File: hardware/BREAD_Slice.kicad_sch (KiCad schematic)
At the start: 16 parts, among them J10 Screw_Terminal_01x02, J11 Screw_Terminal_01x02, J12 Screw_Terminal_01x02, J13 Screw_Terminal_01x02, J14 Screw_Terminal_01x02, J15 Screw_Terminal_01x02, J16 Screw_Terminal_01x02, J2 Screw_Terminal_01x02, J3 Screw_Terminal_01x02, J4 Screw_Terminal_01x02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

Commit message: update schem
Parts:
- removed J10, J11, J12, J13, J14, J16, J2, J3, J4, J5, J6, J7, J8, J9: Screw_Terminal_01x02, symbol Connector:Screw_Terminal_01x02
- added J2, J3, J4, J5, J6, J7, J8, J9: Screw_Terminal_01x04, symbol Connector:Screw_Terminal_01x04
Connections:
- net GND: now also J2.4 (Pin_4), J3.4 (Pin_4), J4.4 (Pin_4), J5.4 (Pin_4), J6.4 (Pin_4), J7.4 (Pin_4), J8.4 (Pin_4), J9.4 (Pin_4)
- net VOUT renamed VFIELD
- net VFIELD: now also J2.3 (Pin_3), J3.3 (Pin_3), J4.3 (Pin_3), J5.3 (Pin_3), J6.3 (Pin_3), J7.3 (Pin_3), J8.3 (Pin_3), J9.3 (Pin_3)
- new net IN1+: J6.1 (Pin_1)
- new net IN1-: J6.2 (Pin_2)
- new net IN2+: J7.1 (Pin_1)
- new net IN2-: J7.2 (Pin_2)
- new net IN3+: J8.1 (Pin_1)
- new net IN3-: J8.2 (Pin_2)
- new net IN4+: J9.1 (Pin_1)
- new net IN4-: J9.2 (Pin_2)
- new net OUT1+: J2.1 (Pin_1)
- new net OUT1-: J2.2 (Pin_2)
- new net OUT2+: J3.1 (Pin_1)
- new net OUT2-: J3.2 (Pin_2)
- new net OUT3+: J4.1 (Pin_1)
- new net OUT3-: J4.2 (Pin_2)
- new net OUT4+: J5.1 (Pin_1)
- new net OUT4-: J5.2 (Pin_2)
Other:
- moved on the sheet: J15, SW3

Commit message: finalize revision of schematic
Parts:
- removed J2, J3, J4, J5, J6, J7, J8, J9: Screw_Terminal_01x04, symbol Connector:Screw_Terminal_01x04
- added J2, J3: Screw_Terminal_01x12, symbol Connector:Screw_Terminal_01x12
- renumbered J15 to J1, SW3 to SW1
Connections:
- net GND: now also J3.12 (Pin_12), J3.3 (Pin_3), J3.6 (Pin_6), J3.9 (Pin_9)
- net IN1+: now also J3.1 (Pin_1)
- net IN1-: now also J3.2 (Pin_2)
- net IN2+: now also J3.4 (Pin_4)
- net IN2-: now also J3.5 (Pin_5)
- net IN3+: now also J3.7 (Pin_7)
- net IN3-: now also J3.8 (Pin_8)
- net IN4+: now also J3.10 (Pin_10)
- net IN4-: now also J3.11 (Pin_11)
- net OUT1+: now also J2.1 (Pin_1)
- net OUT1-: now also J2.2 (Pin_2)
- net OUT2+: now also J2.4 (Pin_4)
- net OUT2-: now also J2.5 (Pin_5)
- net OUT3+: now also J2.7 (Pin_7)
- net OUT3-: now also J2.8 (Pin_8)
- net OUT4+: now also J2.10 (Pin_10)
- net OUT4-: now also J2.11 (Pin_11)
- net VFIELD: now also J2.12 (Pin_12), J2.3 (Pin_3), J2.6 (Pin_6), J2.9 (Pin_9)
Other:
- sheet Isolated Input1 ports: added VCC; removed none
- sheet Isolated Input2 ports: added VCC; removed none
- sheet Isolated Input3 ports: added VCC; removed none
- sheet Isolated Input4 ports: added VCC; removed none
- note added: "Connect GND to IN− for board-referenced (non-isolated) input at IN+. Leave IN− floating for isolated (floating) input; external source must provide return path."
- note added: "Connect VFIELD to OUTx- for wet (VFIELD) contact at OUTx+. Leave VFIELD disconnected and use OUTx− / OUTx+ for dry contact operation."
- note added: "Field Voltage Input Protection"
- note added: "Opto-Isolated Inputs"
- note added: "Reverse and transient voltage protection for external field voltage input."
- note added: "Solid-State Relay Outputs"
- moved on the sheet: J1, SW1

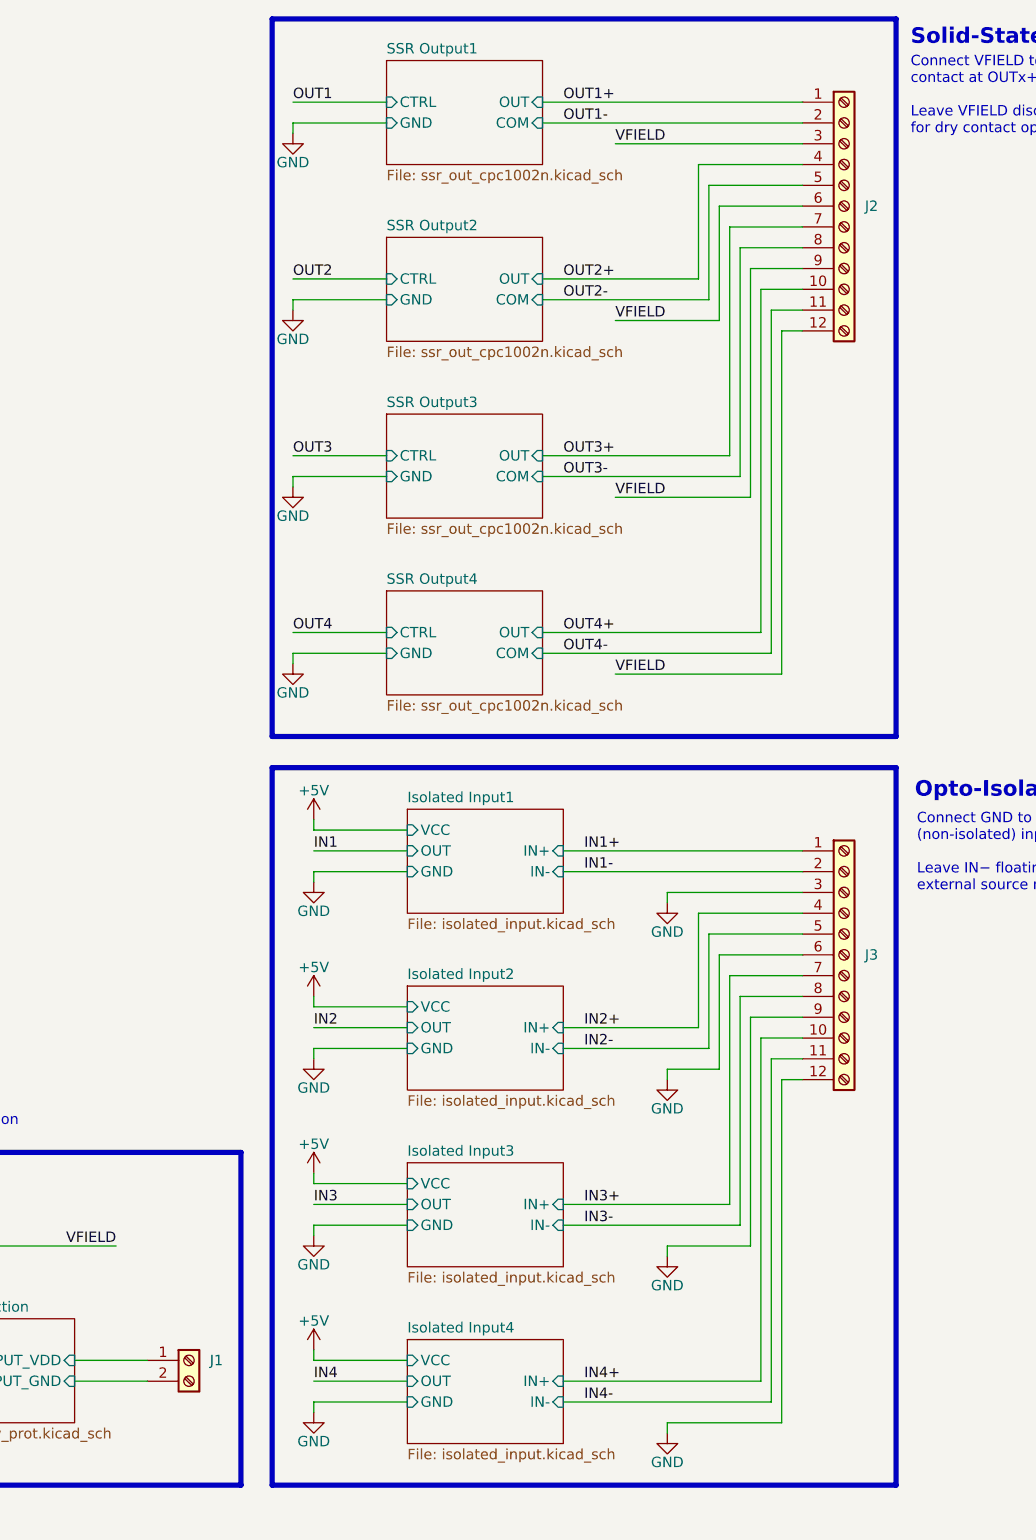
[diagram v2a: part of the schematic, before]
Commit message: revision of symbol attachment and clear out old layout and start new; kml-custom to kmlib-local
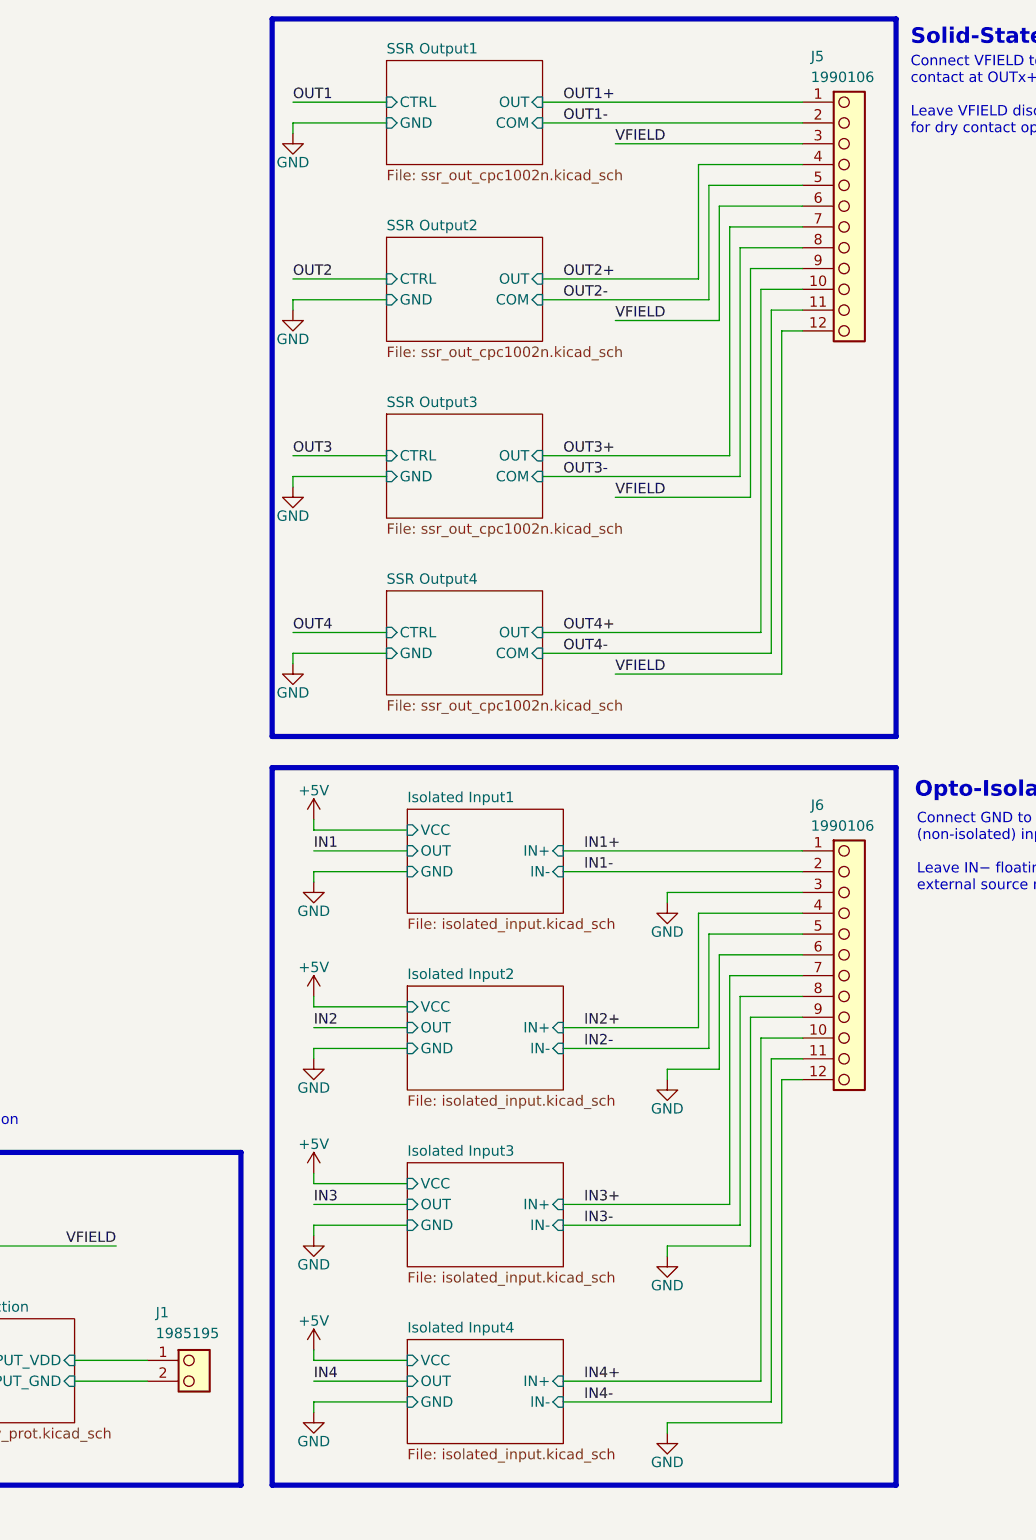
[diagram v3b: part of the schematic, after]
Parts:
- removed J1: Screw_Terminal_01x02, symbol Connector:Screw_Terminal_01x02
- removed J2, J3: Screw_Terminal_01x12, symbol Connector:Screw_Terminal_01x12
- added J1: 1985195, KMLib_Connectors:1985195, symbol KMLib_Connectors:1985195 PTSA Term Push Phoenix Contact
- added J5, J6: 1990106, KMLib_Connectors:1990106, symbol KMLib_Connectors:1990106 PTSA Term Push Phoenix Contact
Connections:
- net GND: now also J6.12, J6.3, J6.6, J6.9
- net IN1+: now also J6.1
- net IN1-: now also J6.2
- net IN2+: now also J6.4
- net IN2-: now also J6.5
- net IN3+: now also J6.7
- net IN3-: now also J6.8
- net IN4+: now also J6.10
- net IN4-: now also J6.11
- net Input Power Protection/INPUT_GND: now also J1.2
- net Input Power Protection/INPUT_VDD: now also J1.1
- net OUT1+: now also J5.1
- net OUT1-: now also J5.2
- net OUT2+: now also J5.4
- net OUT2-: now also J5.5
- net OUT3+: now also J5.7
- net OUT3-: now also J5.8
- net OUT4+: now also J5.10
- net OUT4-: now also J5.11
- net VFIELD: now also J5.12, J5.3, J5.6, J5.9

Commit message: rerouted using PTSA connectors
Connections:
- net OUT1+: now also J5.2; no longer J5.1
- net OUT1-: now also J5.1; no longer J5.2
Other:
- title: (none) -> SLC_IOCT

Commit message: update all to KMLib, untrack backups in gitignore, and revise routing on board to simplify
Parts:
- renumbered J5 to J2, J6 to J3
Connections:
- net +12V: now also SW1.1 (A); no longer SW1.3 (A)
- net +24V: now also SW1.3 (C); no longer SW1.2 (C)
- net VFIELD: now also SW1.2 (B); no longer SW1.1 (B)
- no-connect marks 11 -> 9
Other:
- note added: "Do not use, for i2c backplane"
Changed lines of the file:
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@@
 		)
 	)
+	(text "Do not use, for \ni2c backplane"
+		(exclude_from_sim no)
+		(at 67.564 124.968 0)
+		(effects
+			(font
+				(size 1.27 1.27)
+			)
+		)
+	)
 	(text "Color Scheme Legend:\n----------------------------------------------------------\ncolor		-	value		-	reference\n----------------------------------------------------------\n• Red		-	red3		-	Analog 5V Supply (e.g., for amps, ADC, references)\n• Brown		-	orange1		-	Analog Ground (sensor/amp/ADC ground)\n• Orange	-	orange3		-	Digital 5V Supply (MCU, digital circuits)\n• Black		-	black		-	Digital Ground (MCU ground)\n• Pink		-	magenta3	-	12V Source Supply (from 12V rail on backplane)\n• Blue		-	blue3		-	Clock Signals (oscillator, ADC CLKIN, SPI SCLK)\n• Green		-	green3		-	Analog Signals (amp outputs to ADC + inputs)\n• Yellow	-	yellow3		-	SPI Control (CS, SYNC/RESET, etc.)\n• Purple	-	#A020F0		-	Special/Reference/Control Signals\n• Grey		-	gray2		-	Miscellaneous/Unassigned\n• Teal		-	cyan2		-	Template/Backplane Connections\n----------------------------------------------------------"
 		(exclude_from_sim no)
@@
 	)
 	(no_connect
-		(at 57.15 119.38)
-	)
-	(no_connect
 		(at 57.15 55.88)
 	)
@@
 	)
 	(no_connect
-		(at 57.15 115.57)
-	)
-	(no_connect
 		(at 57.15 90.17)
 	)
@@
 		)
 	)
+	(label "I2C_CLK"
+		(at 57.15 119.38 180)
+		(effects
+			(font
+				(size 1.27 1.27)
+			)
+			(justify right bottom)
+		)
+	)
 	(label "IN3-"
 		(at 135.89 162.56 0)
@@
 		)
 	)
+	(label "I2C_DAT"
+		(at 57.15 115.57 180)
+		(effects
+			(font
+				(size 1.27 1.27)
+			)
+			(justify right bottom)
+		)
+	)
 	(symbol
 		(lib_id "power:GND")
@@
 	)
 	(symbol
-		(lib_name "1990106 PTSA Term Push Phoenix Contact_1")
 		(lib_id "KMLib_Connectors:1990106 PTSA Term Push Phoenix Contact")
 		(at 167.64 144.78 0)
@@
 		(on_board yes)
 		(dnp no)
-		(property "Reference" "J6"
+		(property "Reference" "J3"
 			(at 163.576 111.252 0)
 			(effects
@@
 			(project "BREAD_Slice"
 				(path "/66043bca-a260-4915-9fce-8a51d324c687"
-					(reference "J6")
+					(reference "J3")
 					(unit 1)
 				)
@@
 		(on_board yes)
 		(dnp no)
-		(property "Reference" "J5"
+		(property "Reference" "J2"
 			(at 163.576 19.812 0)
 			(effects
@@
 			(project ""
 				(path "/66043bca-a260-4915-9fce-8a51d324c687"
-					(reference "J5")
+					(reference "J2")
 					(unit 1)
 				)

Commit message: added dip switches to IOCT
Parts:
- added SW3: SW_DIP_x04, Button_Switch_SMD:SW_DIP_SPSTx04_Slide_9.78x12.34mm_W8.61mm_P2.54mm, symbol Switch:SW_DIP_x04
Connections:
- net OUT1: now also SW3.4
- net OUT2: now also SW3.3
- net OUT3: now also SW3.2
- net OUT4: now also SW3.1
- new net ESTOP: SW3.5, SW3.6, SW3.7, SW3.8
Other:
- sheet slice_template ports: added ESTOP; removed none
